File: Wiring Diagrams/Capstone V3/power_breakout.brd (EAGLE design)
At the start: 75.9 x 44.4 mm, 24 parts, among them J1 RASPBERRYPI-40-PIN-GPIO_PTH_N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, U1 2N7000RLRAG

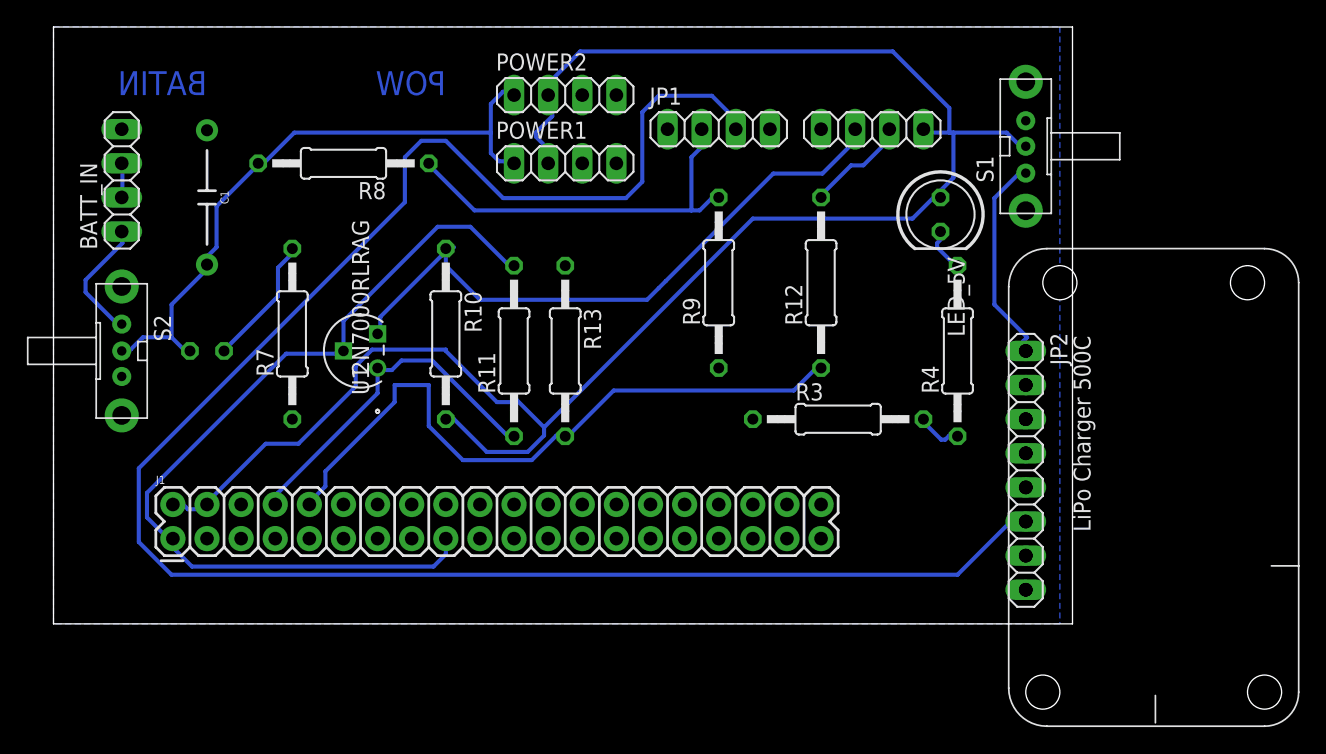
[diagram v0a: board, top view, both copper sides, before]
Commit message: Modified power supply board to remove extra holes
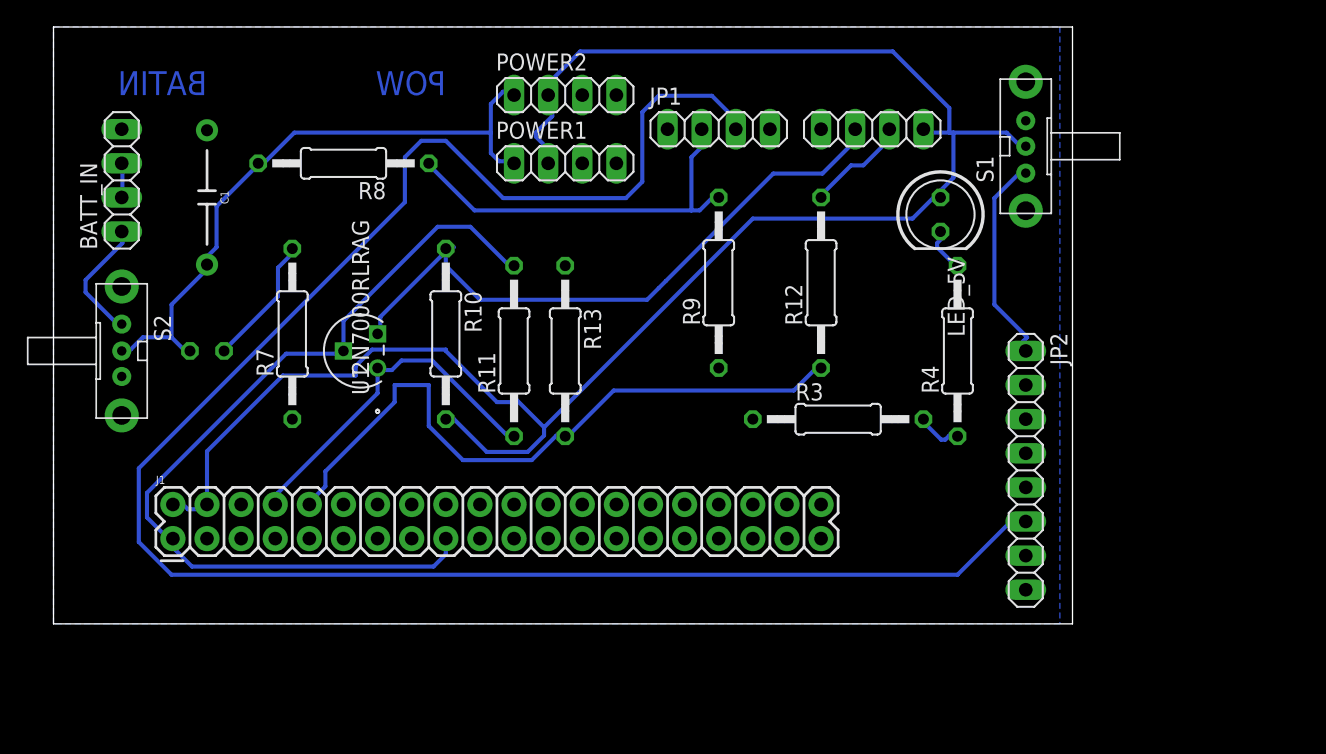
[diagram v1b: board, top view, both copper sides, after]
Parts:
- removed U$1: POWERBOOST500C, jos-ph:POWERBOOST500
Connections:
- net GND: no longer U$1.2, U$1.7
- net N$30: no longer U$1.8
- net N$4: no longer U$1.6
- net N$5: no longer U$1.5
- net N$6: no longer U$1.4
- net N$7: no longer U$1.1
- net V_BATT: no longer U$1.3
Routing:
- net 5V: track 137.2 -> 138.9 mm
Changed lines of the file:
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@@
 <attribute name="NAME" x="31.61" y="23.02" size="1.27" layer="21" font="vector" rot="R270"/>
 </element>
-<element name="U$1" library="jos-ph" package="POWERBOOST500" value="POWERBOOST500C" x="116.84" y="-7.62" smashed="yes" rot="R90"/>
 <element name="U1" library="2N7000RLRAG" package="TO-92" value="2N7000RLRAG" x="45.72" y="21.59" smashed="yes" rot="R90">
 <attribute name="BUILT_BY" value="EMA_UL_Team" x="100.33" y="80.01" size="1.778" layer="27" rot="R90" display="off"/>
@@
 <contactref element="POWER1" pad="4"/>
 <contactref element="POWER2" pad="4"/>
-<contactref element="U$1" pad="7"/>
-<contactref element="U$1" pad="2"/>
 <contactref element="R3" pad="1"/>
 <polygon width="0.1524" layer="16">
@@
 <wire x1="43.18" y1="6.35" x2="48.26" y2="8.89" width="0" layer="19" extent="1-1"/>
 <wire x1="38.1" y1="8.89" x2="43.18" y2="6.35" width="0" layer="19" extent="1-1"/>
-<wire x1="41.91" y1="15.24" x2="38.1" y2="8.89" width="0" layer="19" extent="1-1"/>
 </signal>
 <signal name="5V">
@@
 <wire x1="88.0872" y1="30.1752" x2="76.2" y2="30.1752" width="0.3048" layer="16"/>
 <wire x1="89.916" y1="32.004" x2="88.0872" y2="30.1752" width="0.3048" layer="16"/>
-<wire x1="39.9288" y1="13.4112" x2="35.6616" y2="9.144" width="0.3048" layer="16"/>
-<wire x1="42.3672" y1="13.4112" x2="39.9288" y2="13.4112" width="0.3048" layer="16"/>
-<wire x1="46.6344" y1="17.6784" x2="42.3672" y2="13.4112" width="0.3048" layer="16"/>
-<wire x1="46.6344" y1="19.2024" x2="46.6344" y2="17.6784" width="0.3048" layer="16"/>
+<wire x1="41.1988" y1="18.4912" x2="35.56" y2="12.8524" width="0.3048" layer="16"/>
+<wire x1="46.6344" y1="18.4912" x2="41.1988" y2="18.4912" width="0.3048" layer="16"/>
+<wire x1="46.6344" y1="19.2024" x2="46.6344" y2="18.4912" width="0.3048" layer="16"/>
 <wire x1="47.8536" y1="20.4216" x2="46.6344" y2="19.2024" width="0.3048" layer="16"/>
-<wire x1="35.6616" y1="9.144" x2="35.56" y2="8.89" width="0.3048" layer="16"/>
+<wire x1="35.56" y1="12.8524" x2="35.56" y2="8.89" width="0.3048" layer="16"/>
 <wire x1="91.1352" y1="33.2232" x2="91.1352" y2="36.576" width="0.3048" layer="16"/>
 <wire x1="89.916" y1="32.004" x2="91.1352" y2="33.2232" width="0.3048" layer="16"/>
@@
 <signal name="N$30">
 <contactref element="S1" pad="1"/>
-<contactref element="U$1" pad="8"/>
 <contactref element="JP2" pad="1"/>
 <wire x1="96.012" y1="33.528" x2="96.3168" y2="33.528" width="0.3048" layer="16"/>
@@
 </signal>
 <signal name="V_BATT">
-<contactref element="U$1" pad="3"/>
 <contactref element="JP2" pad="6"/>
 <contactref element="JP1" pad="3"/>
@@
 </signal>
 <signal name="N$4">
-<contactref element="U$1" pad="6"/>
 <contactref element="JP2" pad="3"/>
 </signal>
 <signal name="N$5">
-<contactref element="U$1" pad="5"/>
 <contactref element="JP2" pad="4"/>
 </signal>
 <signal name="N$6">
-<contactref element="U$1" pad="4"/>
 <contactref element="JP2" pad="5"/>
 </signal>
 <signal name="N$7">
-<contactref element="U$1" pad="1"/>
 <contactref element="JP2" pad="8"/>
 </signal>
